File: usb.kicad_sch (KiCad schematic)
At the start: 55 parts, among them J901 AU-Y1008-2-BLK, J902 AU-Y1008-2-BLK, U901 USB2514B/M2, U902 AP22966DC8-7, U903 AP22966DC8-7, U904 USBLC6-2SC6, U905 USBLC6-2SC6, U906 USBLC6-2SC6, U907 USBLC6-2SC6, Y901 24 MHz

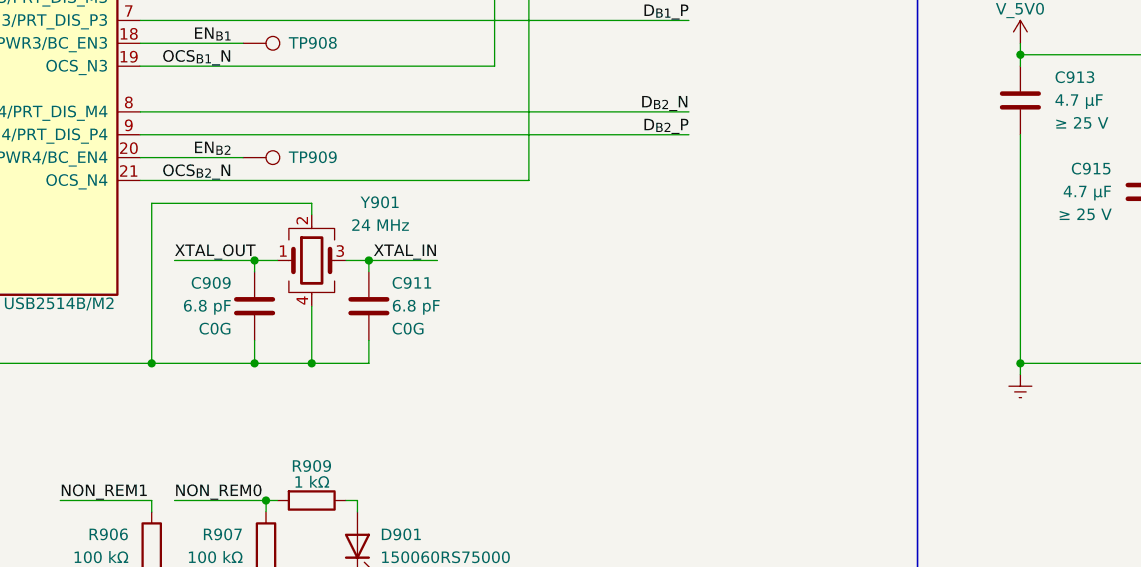
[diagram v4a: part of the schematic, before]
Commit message: Refactor MPU and USB
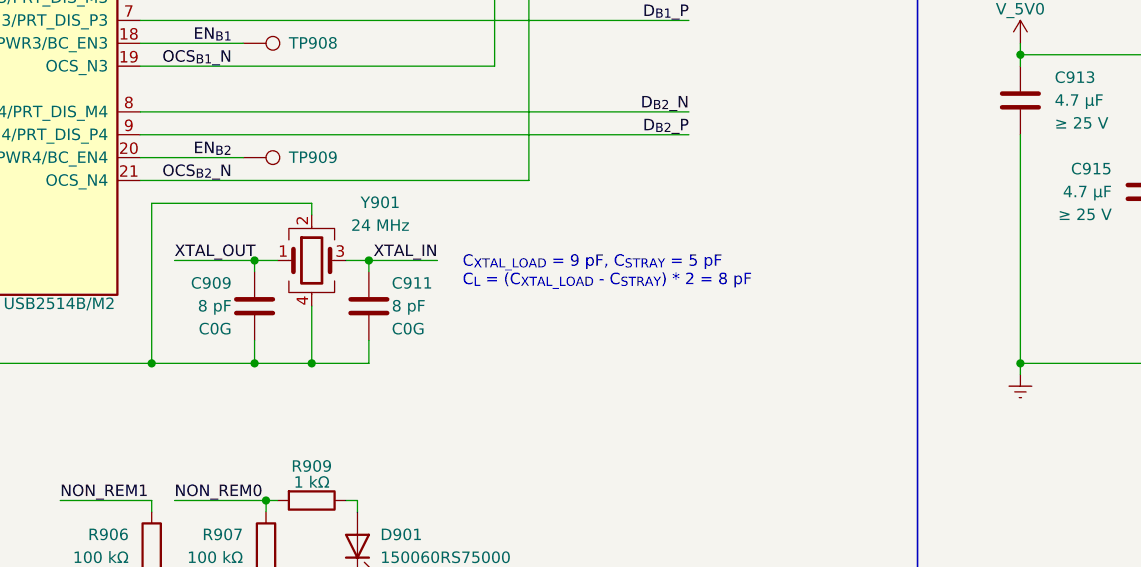
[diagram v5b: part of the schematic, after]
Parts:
- C909, C911: value 6.8 pF -> 8 pF
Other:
- note added: "C_{XTAL_LOAD} = 9 pF, C_{STRAY} = 5 pF C_{L} = (C_{XTAL_LOAD} - C_{STRAY}) * 2 = 8 pF"
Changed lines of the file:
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@@
 		)
 	)
+	(text "C_{XTAL_LOAD} = 9 pF, C_{STRAY} = 5 pF\nC_{L} = (C_{XTAL_LOAD} - C_{STRAY}) * 2 = 8 pF"
+		(exclude_from_sim no)
+		(at 165.354 177.8 0)
+		(effects
+			(font
+				(size 1.27 1.27)
+			)
+			(justify left)
+		)
+	)
 	(text_box "USB hub controller"
 		(exclude_from_sim no)
@@
 			)
 		)
-		(property "Value" "6.8 pF"
+		(property "Value" "8 pF"
 			(at 139.7 181.61 0)
 			(effects
@@
 			)
 		)
-		(property "Value" "6.8 pF"
+		(property "Value" "8 pF"
 			(at 157.48 181.61 0)
 			(effects

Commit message: Refactor DDR and USB
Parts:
- renumbered R909 to R908, R908 to R909
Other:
- moved on the sheet: R909, R910, R911, R912

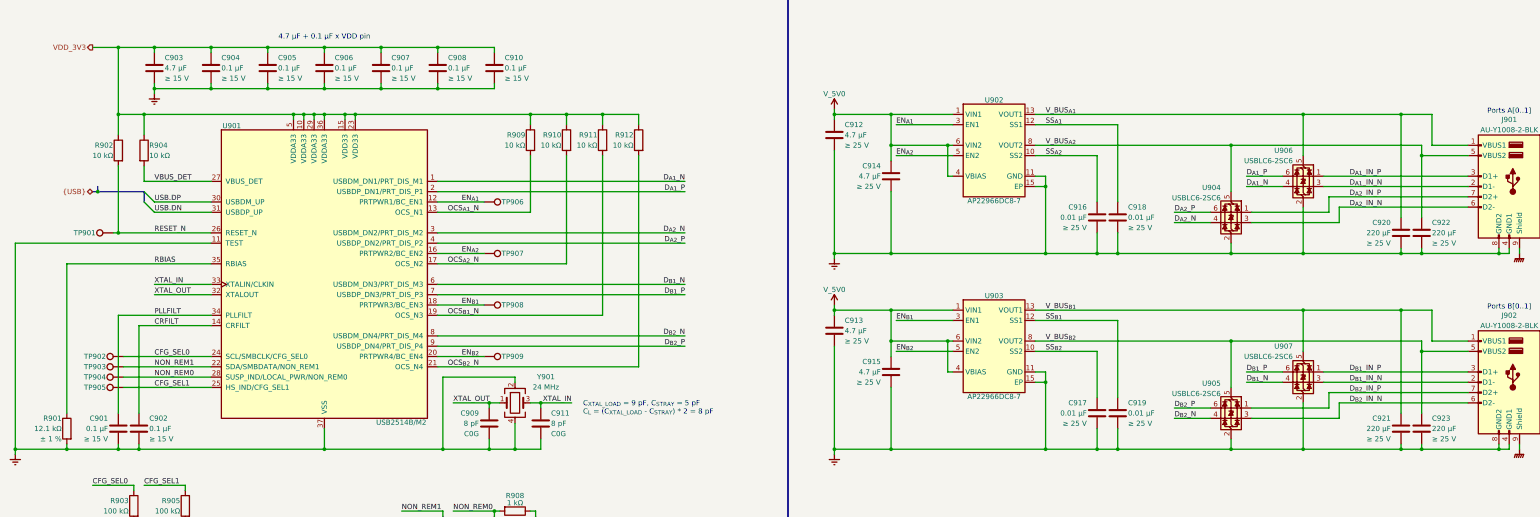
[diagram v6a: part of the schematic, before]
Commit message: Fix component values
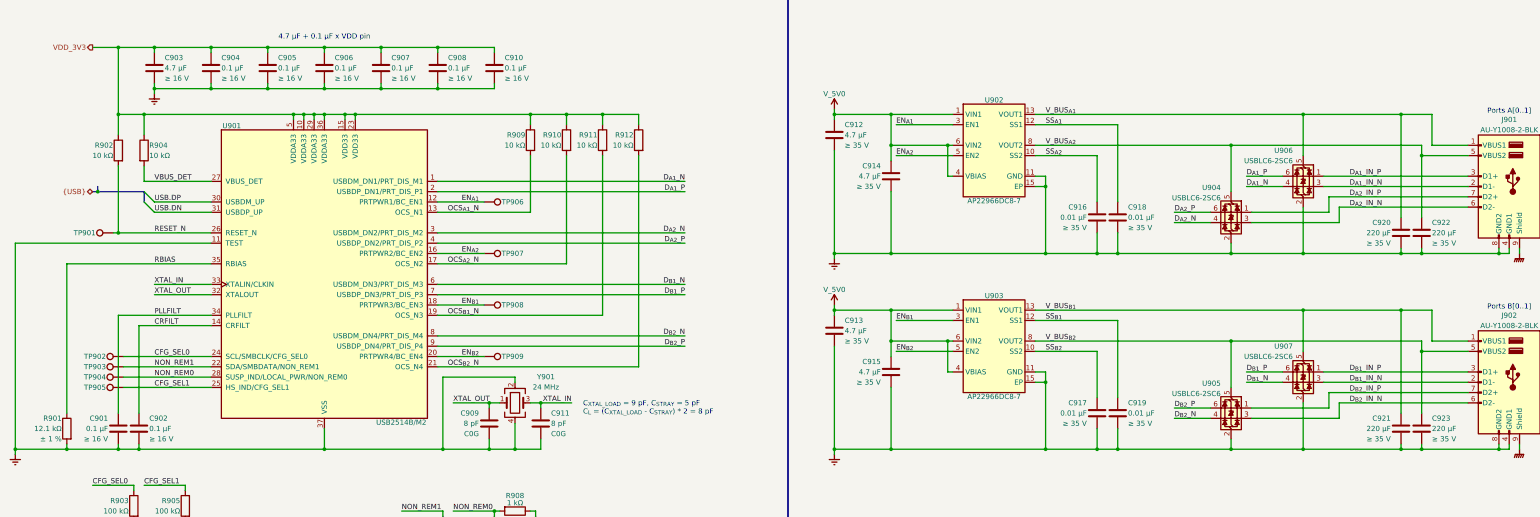
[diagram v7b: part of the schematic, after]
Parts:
- C901, C902, C903, C904, C905, C906, C907, C908, C910: Voltage rating ≥ 15 V -> ≥ 16 V
- C912, C913, C914, C915, C916, C917, C918, C919, C920, C921, C922, C923: Voltage rating ≥ 25 V -> ≥ 35 V
